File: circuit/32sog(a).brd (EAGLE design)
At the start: 54 x 34 mm, 17 parts, among them IC1 MEGA8-P, K1 PG203J, X1 16.0

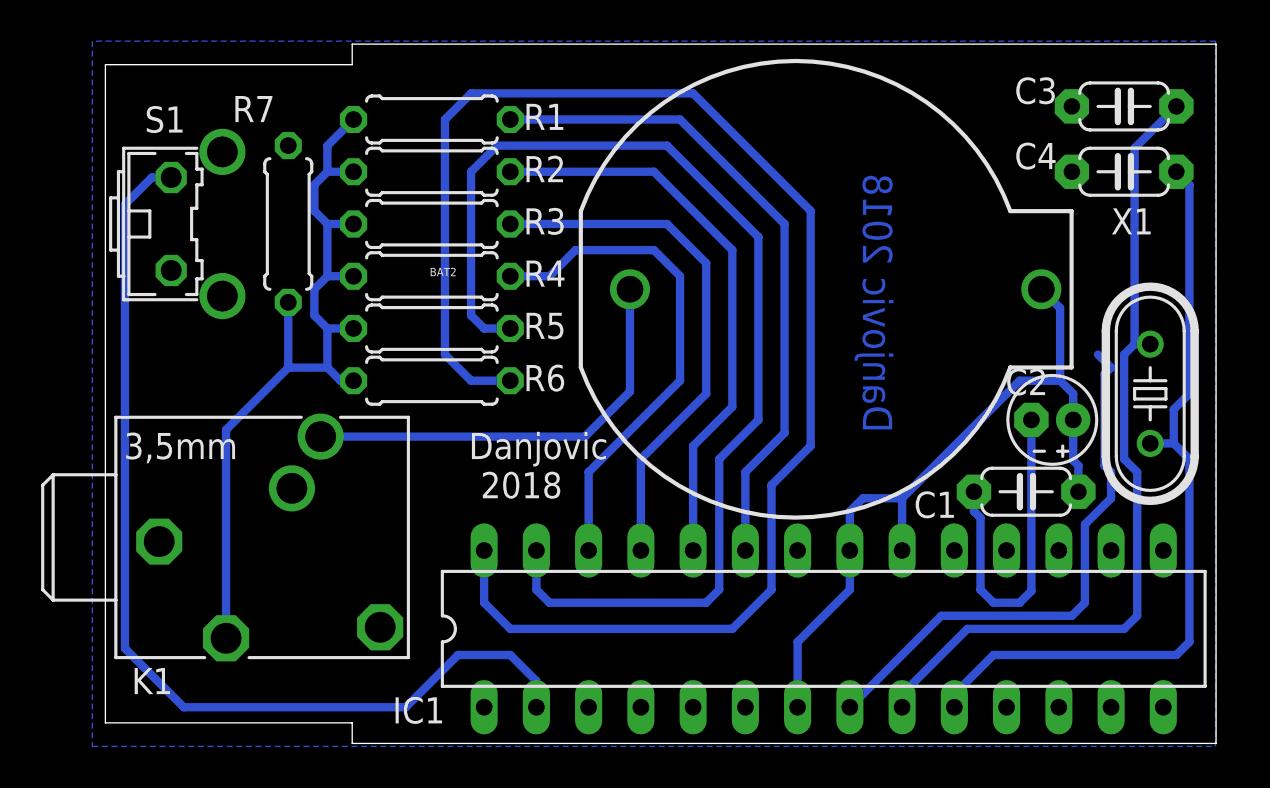
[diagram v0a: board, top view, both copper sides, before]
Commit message: Added pull-up resistor on RESET line
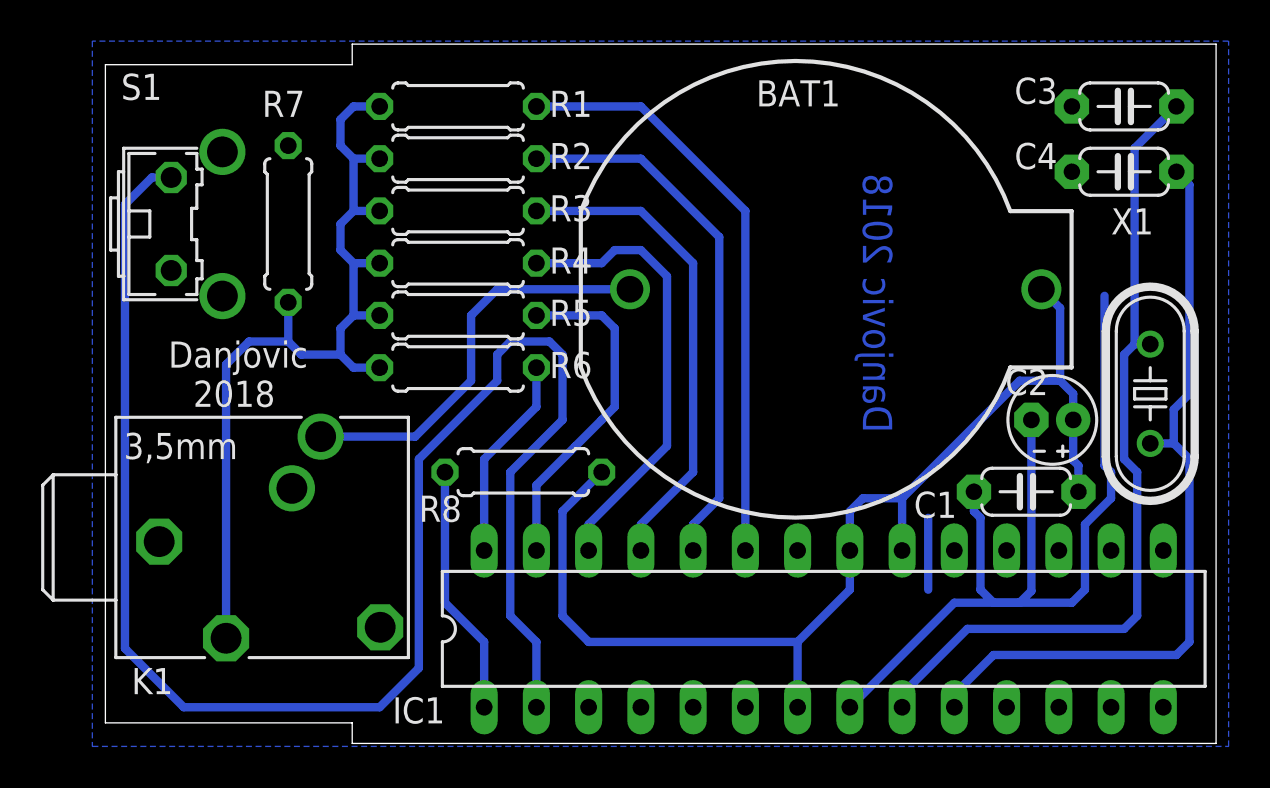
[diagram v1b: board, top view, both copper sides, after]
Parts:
- added R8: 10k, rcl:0207/7
- moved R2 1.42 mm to (17.8, 51.4)
- moved R3 1.42 mm to (17.8, 48.9)
- moved R1 1.42 mm to (17.8, 54.0)
- moved R4 1.42 mm to (17.8, 46.4)
- moved R5 1.42 mm to (17.8, 43.8)
- moved R6 1.42 mm to (17.8, 41.3)
- renumbered BAT2 to BAT1
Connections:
- new net N$3: IC1.1, R8.2
- net VCC: now also R8.1
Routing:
- net N$7: track 72.8 -> 9.94 mm
- net N$4: track 54.7 -> 16.4 mm
- net N$12: track 48.4 -> 79.9 mm
- net VCC: track 36.6 -> 56.3 mm
- net N$3: track 0.00 -> 12.2 mm
- net GND: track 42.8 -> 48.4 mm
- net N$10: track 39.7 -> 43.4 mm
- net N$1: track 32.1 -> 28.8 mm
- net N$6: track 24.5 -> 22.1 mm
- net N$2: track 25.6 -> 23.7 mm
- net N$5: track 27.8 -> 26.2 mm
- net N$9: track 20.9 -> 19.9 mm
